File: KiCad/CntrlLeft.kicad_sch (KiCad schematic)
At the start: 4 parts, among them SW1 SW_Push, SW6 SW_Push, SW8 SW_Push, SW9 SW_Push

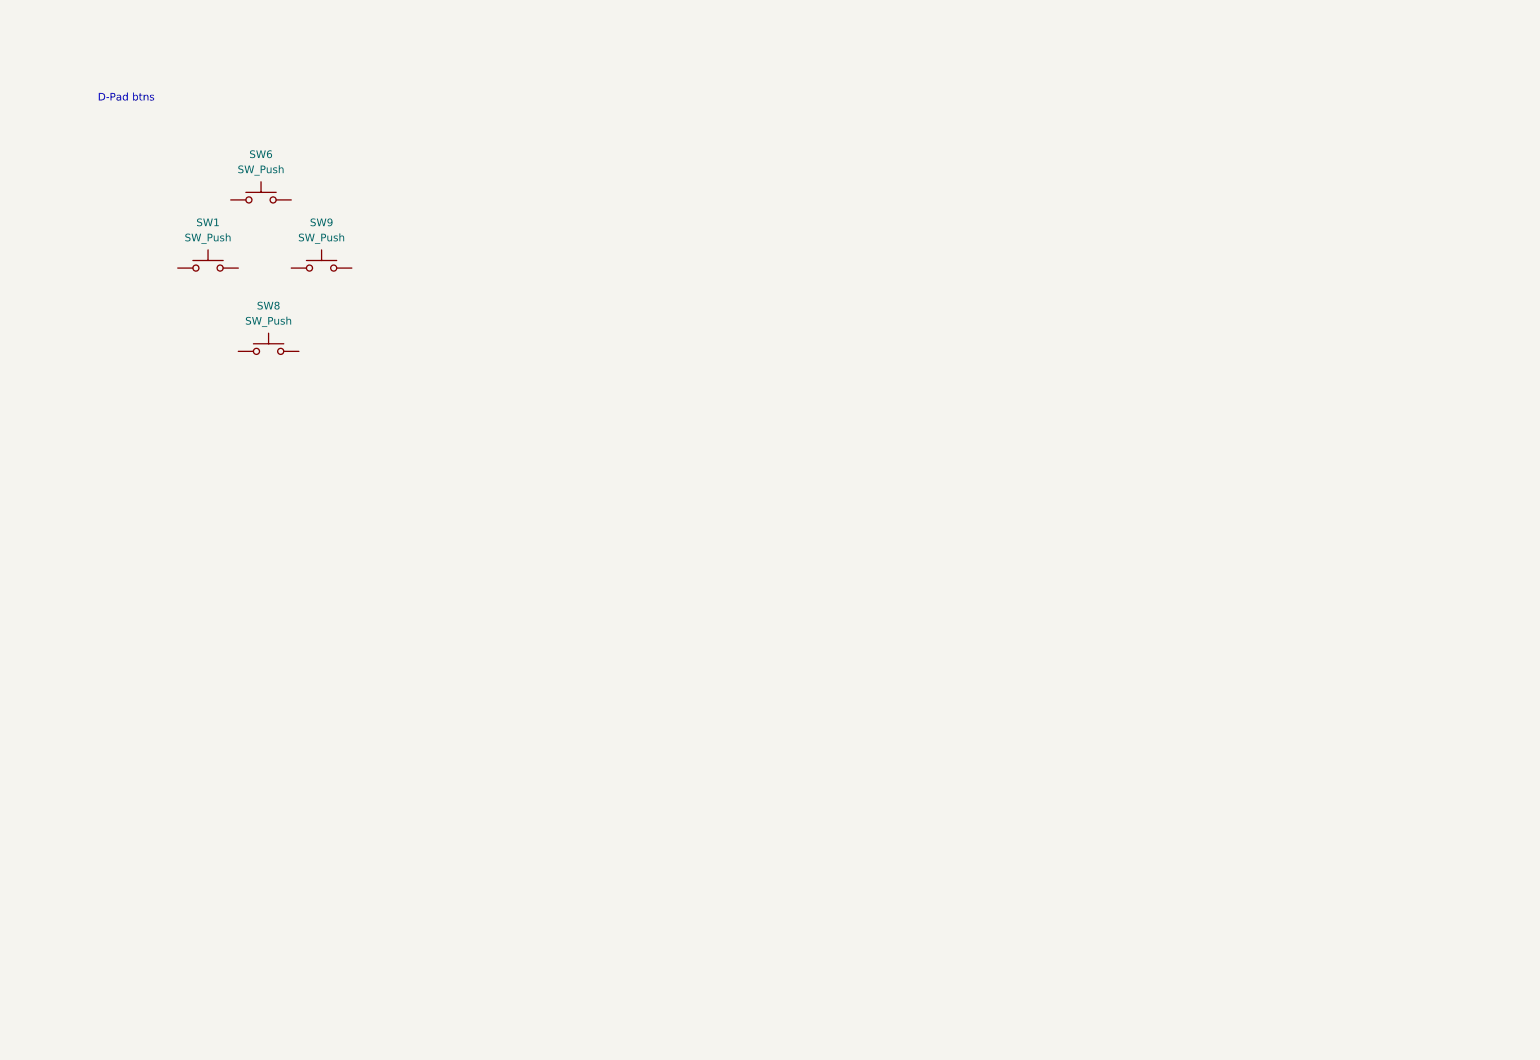
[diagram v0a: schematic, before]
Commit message: added hierachical sheets to controllers
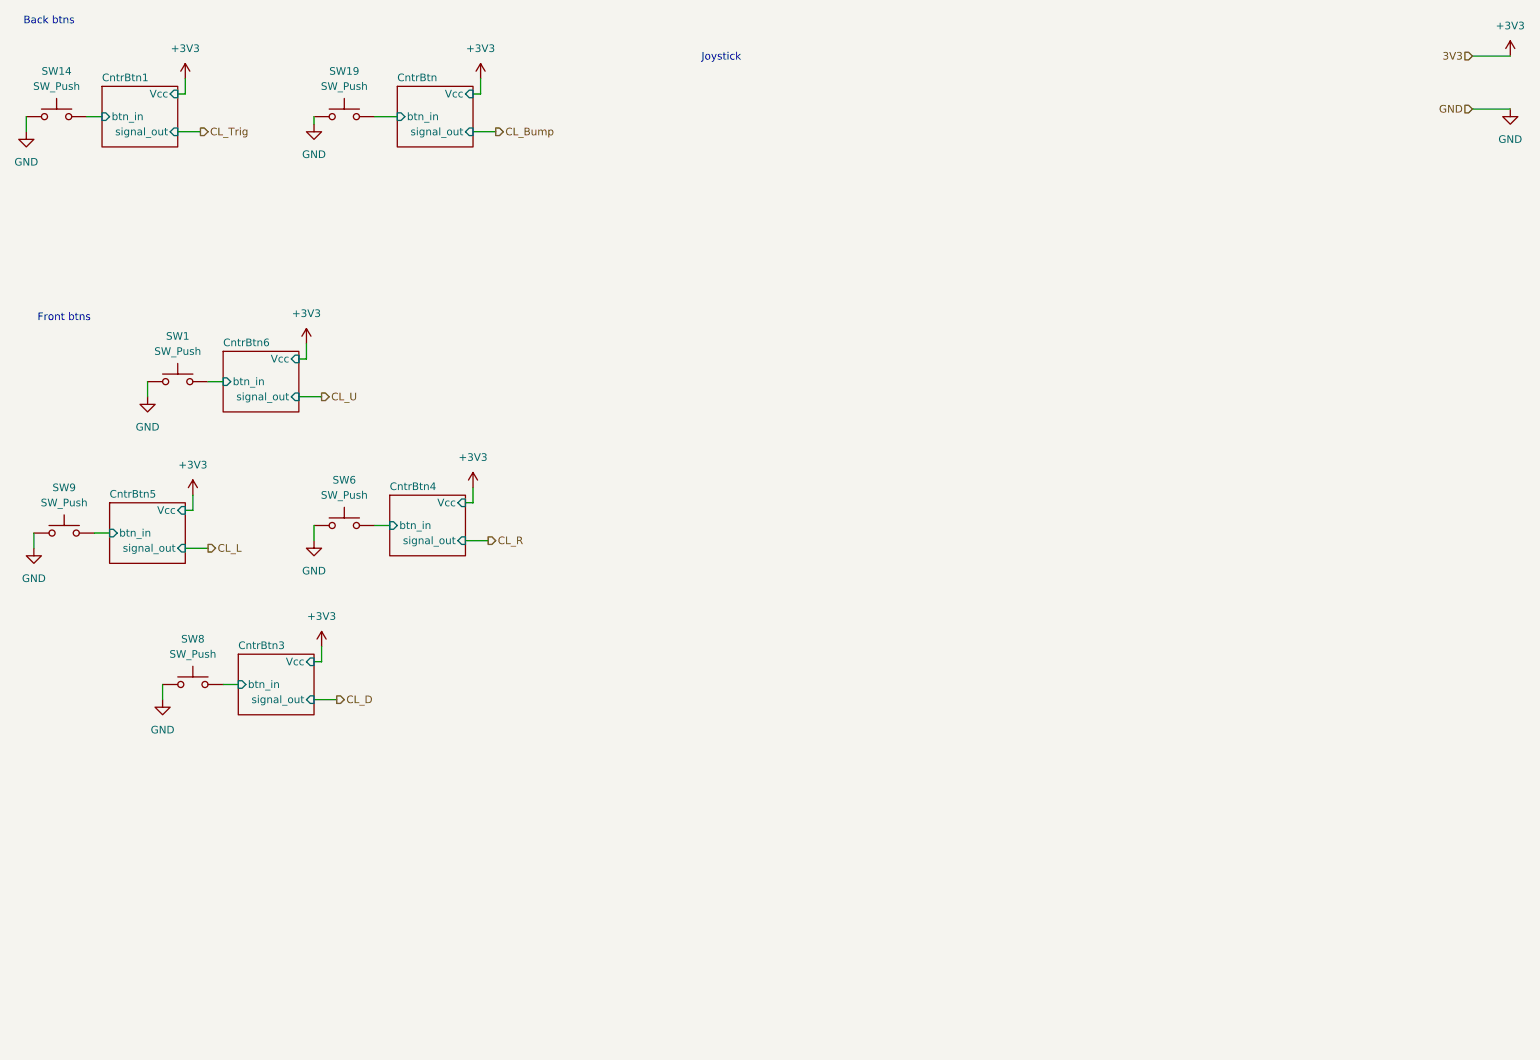
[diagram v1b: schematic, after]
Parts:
- added SW14, SW19: SW_Push, symbol CM5_HighSpeedBreakout:SW_Push
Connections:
- net GND: now reaches SW8.1
- net GND: now also SW6.1, SW9.1, SW14.1, SW19.1
- net CntrBtn3/btn_in: now reaches SW8.2
- net CntrBtn4/btn_in: now reaches SW6.2
- net CntrBtn6/btn_in: now reaches SW1.2
- net CntrBtn5/btn_in: now reaches SW9.2
- new net CntrBtn/btn_in: SW19.2
- new net CntrBtn1/btn_in: SW14.2
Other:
- added sheet CntrBtn (CntrBtn.kicad_sch)
- added sheet CntrBtn1 (CntrBtn.kicad_sch)
- added sheet CntrBtn3 (CntrBtn.kicad_sch)
- added sheet CntrBtn4 (CntrBtn.kicad_sch)
- added sheet CntrBtn5 (CntrBtn.kicad_sch)
- added sheet CntrBtn6 (CntrBtn.kicad_sch)
- note added: "Back btns"
- note added: "Front btns"
- note added: "Joystick"
- note removed: "D-Pad btns"
- moved on the sheet: SW1, SW6, SW8, SW9

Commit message: redid button pull up. Added initial joystick and display symbols
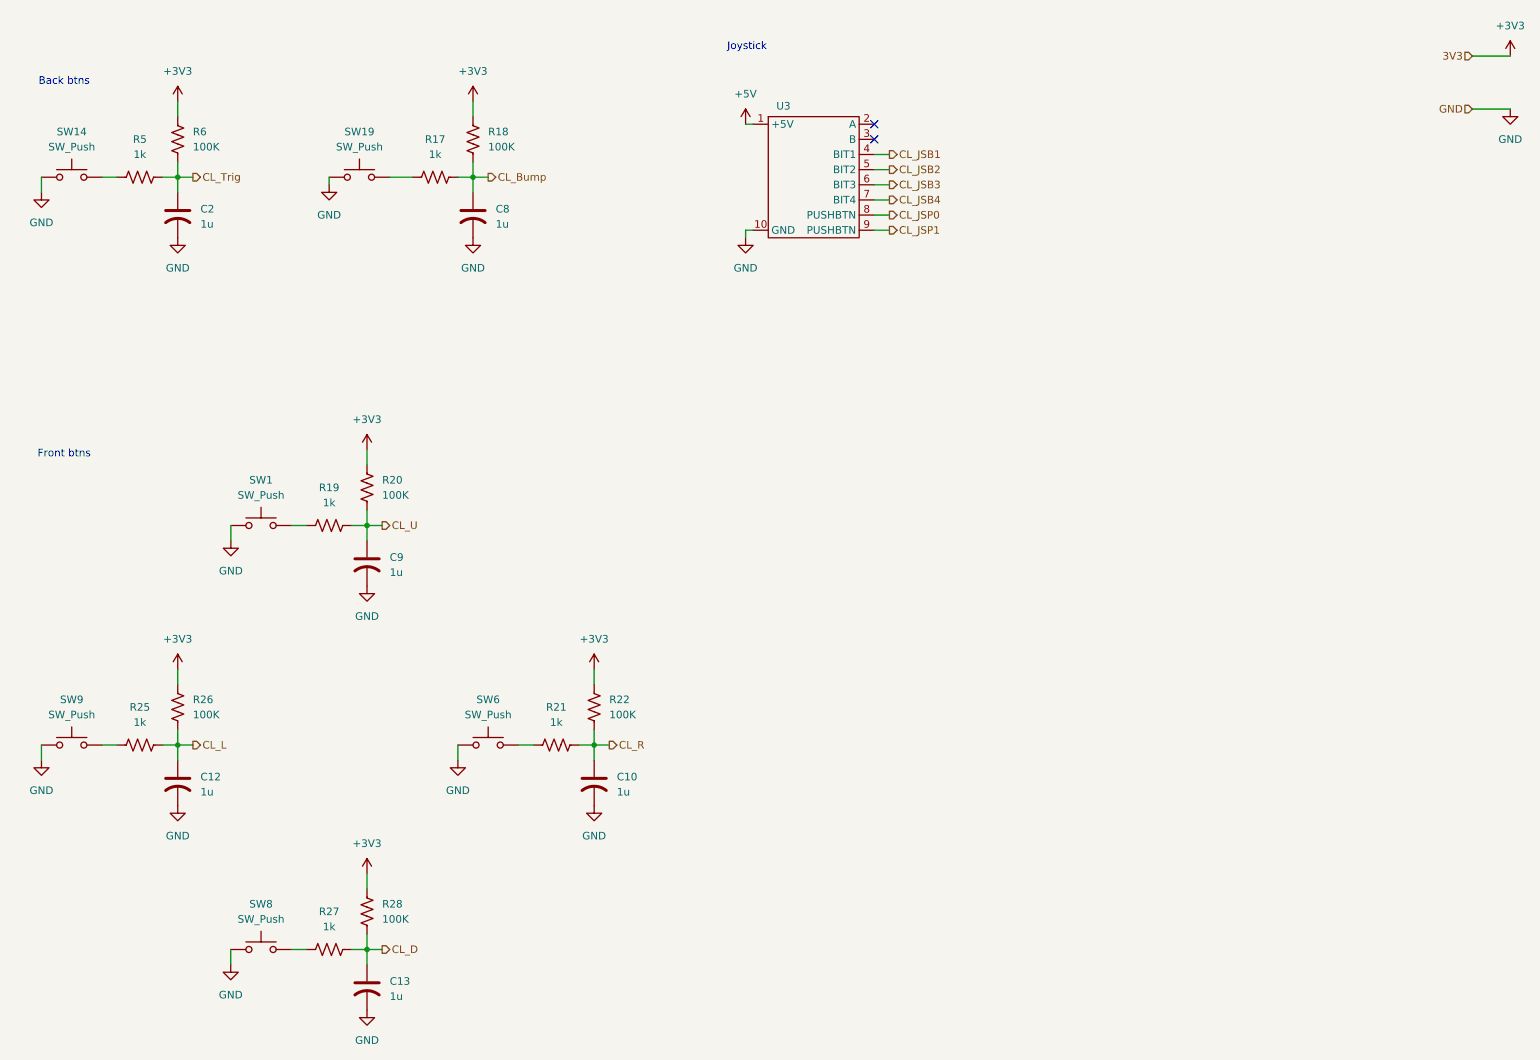
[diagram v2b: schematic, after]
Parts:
- added C10, C12, C13, C2, C8, C9: 1u, symbol Device:C_US
- added R17, R19, R21, R25, R27, R5: 1k, symbol Device:R_US
- added R18, R20, R22, R26, R28, R6: 100K, symbol Device:R_US
- added U3: ~, symbol SBC_handheld:joystick_3axis
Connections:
- net +3V3: now also R18.1, R20.1, R22.1, R26.1, R28.1, R6.1
- net CL_Bump: now also C8.1, R17.2, R18.2
- net CL_D: now also C13.1, R27.2, R28.2
- net CL_L: now also C12.1, R25.2, R26.2
- net CL_R: now also C10.1, R21.2, R22.2
- net CL_Trig: now also C2.1, R5.2, R6.2
- net CL_U: now also C9.1, R19.2, R20.2
- net GND: now also C10.2, C12.2, C13.2, C2.2, C8.2, C9.2, U3.10 (GND)
- net CntrBtn/btn_in: no longer names the net of SW19.2
- net CntrBtn/btn_in: now also R17.1
- net CntrBtn1/btn_in: no longer names the net of SW14.2
- net CntrBtn1/btn_in: now also R5.1
- net CntrBtn3/btn_in: no longer names the net of SW8.2
- net CntrBtn3/btn_in: now also R27.1
- net CntrBtn4/btn_in: no longer names the net of SW6.2
- net CntrBtn4/btn_in: now also R21.1
- net CntrBtn5/btn_in: no longer names the net of SW9.2
- net CntrBtn5/btn_in: now also R25.1
- net CntrBtn6/btn_in: no longer names the net of SW1.2
- net CntrBtn6/btn_in: now also R19.1
- new net +5V: U3.1 (+5V)
- new net CL_JSB1: U3.4 (BIT1)
- new net CL_JSB2: U3.5 (BIT2)
- new net CL_JSB3: U3.6 (BIT3)
- new net CL_JSB4: U3.7 (BIT4)
- new net CL_JSP0: U3.8 (PUSHBTN)
- new net CL_JSP1: U3.9 (PUSHBTN)
- no-connect marks 0 -> 2
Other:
- removed sheet CntrBtn
- removed sheet CntrBtn1
- removed sheet CntrBtn3
- removed sheet CntrBtn4
- removed sheet CntrBtn5
- removed sheet CntrBtn6
- moved on the sheet: SW1, SW14, SW19, SW6, SW8, SW9
